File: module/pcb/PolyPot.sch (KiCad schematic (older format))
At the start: 40 parts, among them J1 V_BAT_1S, J2 PROG/DEBUG, J3 HUMIDITY_CONN, J4 TOF_DIST_SENS, J5 M3, J6 M3, J7 M3, J8 M3, J9 LUMINOSITY_CONN, M1 DC_WATER_PUMP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

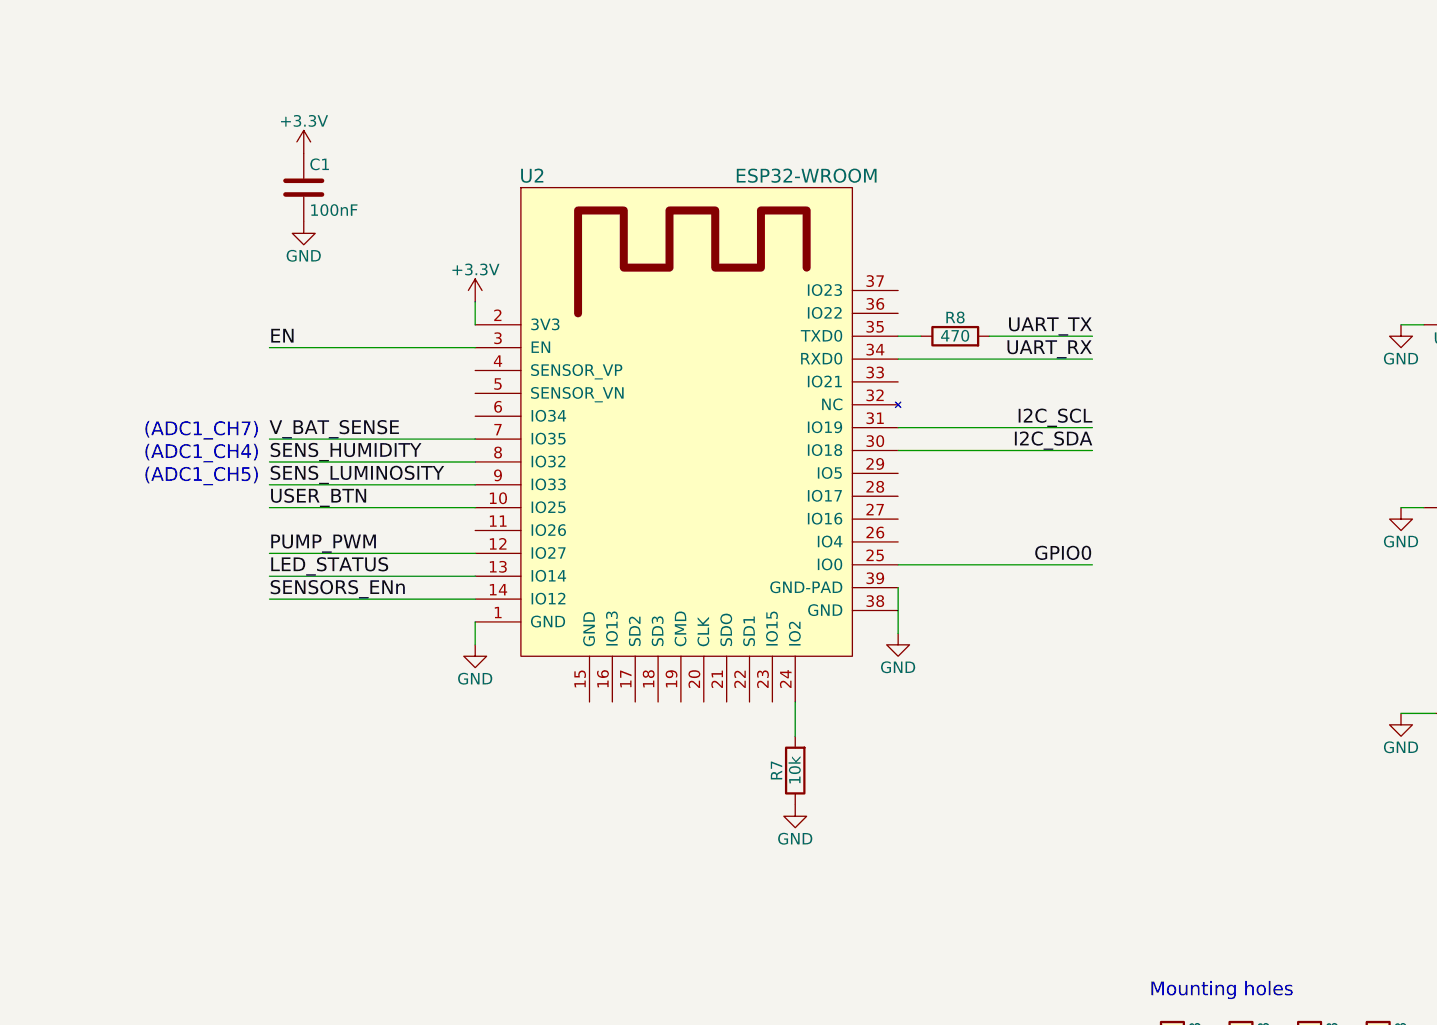
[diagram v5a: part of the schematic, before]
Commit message: Replaced ESP32-WROOM with ESP32-S
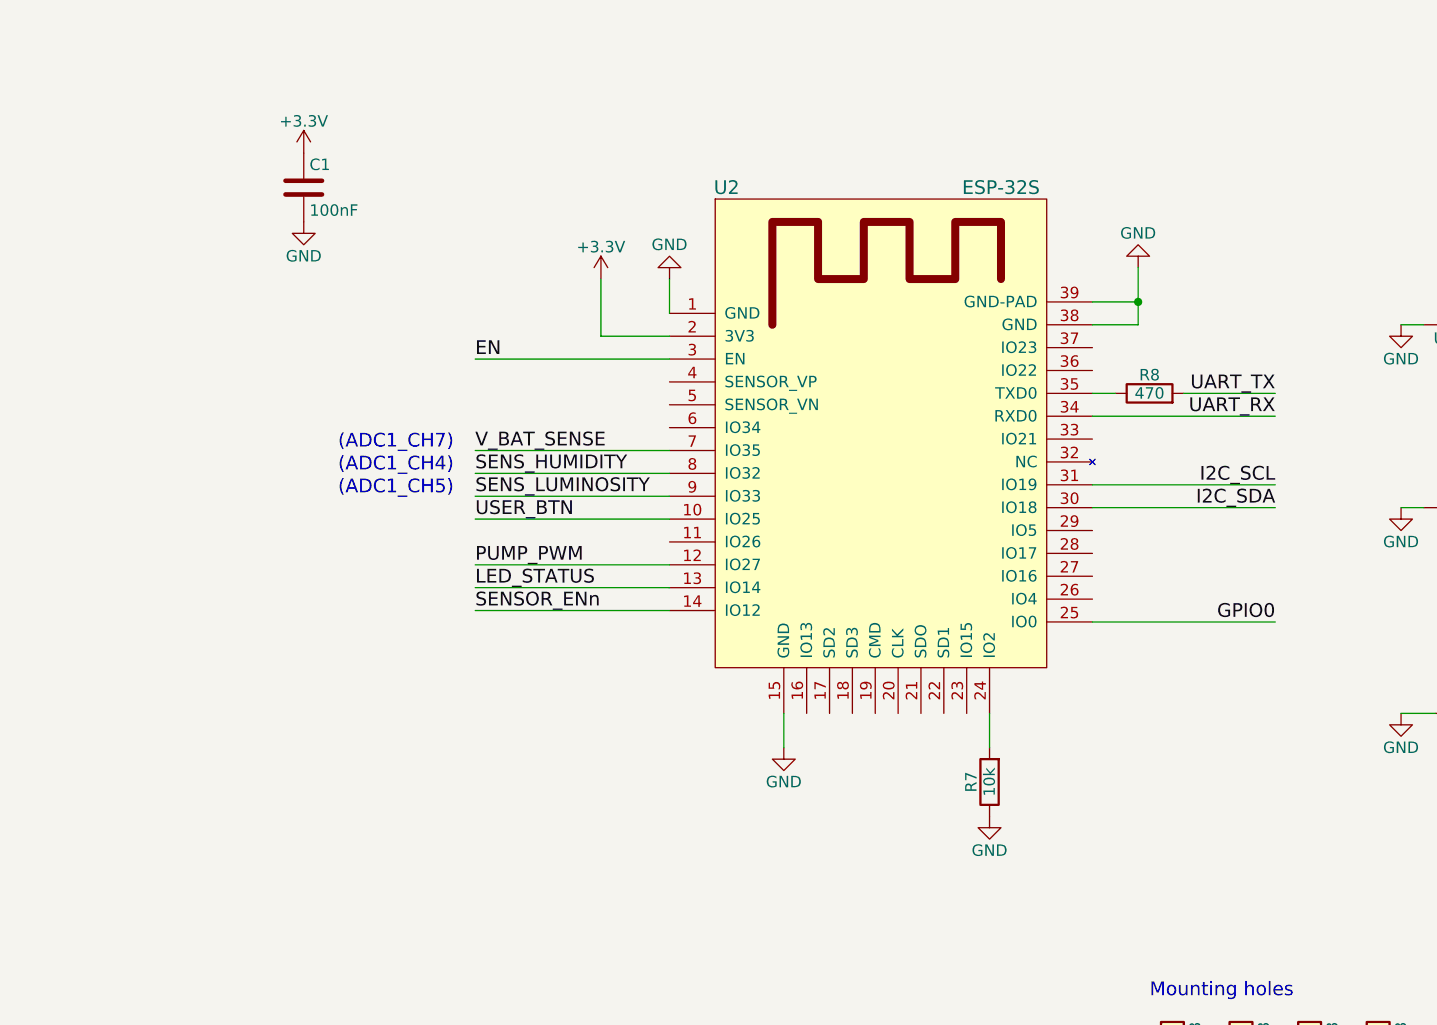
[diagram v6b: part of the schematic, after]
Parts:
- removed U2: ESP32-WROOM, PolyPot:ESP32-WROOM, symbol ESP32-WROOM
- added U2: ESP-32S, ESP32-footprints-Lib:ESP-32S, symbol ESP-32S
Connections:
- net +3V3: now also U2.2 (3V3)
- net EN: now also U2.3 (EN)
- net GND: now also U2.1 (GND), U2.15 (GND), U2.38 (GND), U2.39 (GND-PAD)
- net GPIO0: now also U2.25 (IO0)
- net I2C_SCL: now also U2.31 (IO19)
- net I2C_SDA: now also U2.30 (IO18)
- net LED_STATUS: now also U2.13 (IO14)
- net PUMP_PWM: now also U2.12 (IO27)
- net SENS_HUMIDITY: now also U2.8 (IO32)
- net SENS_LUMINOSITY: now also U2.9 (IO33)
- net UART_RX: now also U2.34 (RXD0)
- net USER_BTN: now also U2.10 (IO25)
- net V_BAT_SENSE: now also U2.7 (IO35)
- net at R7.2: now also U2.24 (IO2)
- net at R8.1: now also U2.35 (TXD0)
- new net SENSOR_ENn: U2.14 (IO12)
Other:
- moved on the sheet: R7, R8

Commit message: Added the PWM driver and routed it on the PCB
There might be some issues with the path for library for ESP32-S. You might need to respecify the path to "ESP32-footprints-Lib.pretty" in the PCB editor library manager.
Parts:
- removed Q1: Q_NMOS_DGS, TO_SOT_Packages_SMD:SOT-23, symbol Q_NMOS_DGS
- added C5: 10uF, Capacitors_SMD:C_0805_HandSoldering, symbol C
- added R10: 10k, Resistors_SMD:R_0603_HandSoldering, symbol R
- added U4: BD6211F-E2, Housings_SOIC:SO-8_5.3x6.2mm_Pitch1.27mm, symbol BD6211F-E2
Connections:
- wire segments 77 -> 88
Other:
- moved on the sheet: JP2, M1, Q2, R2

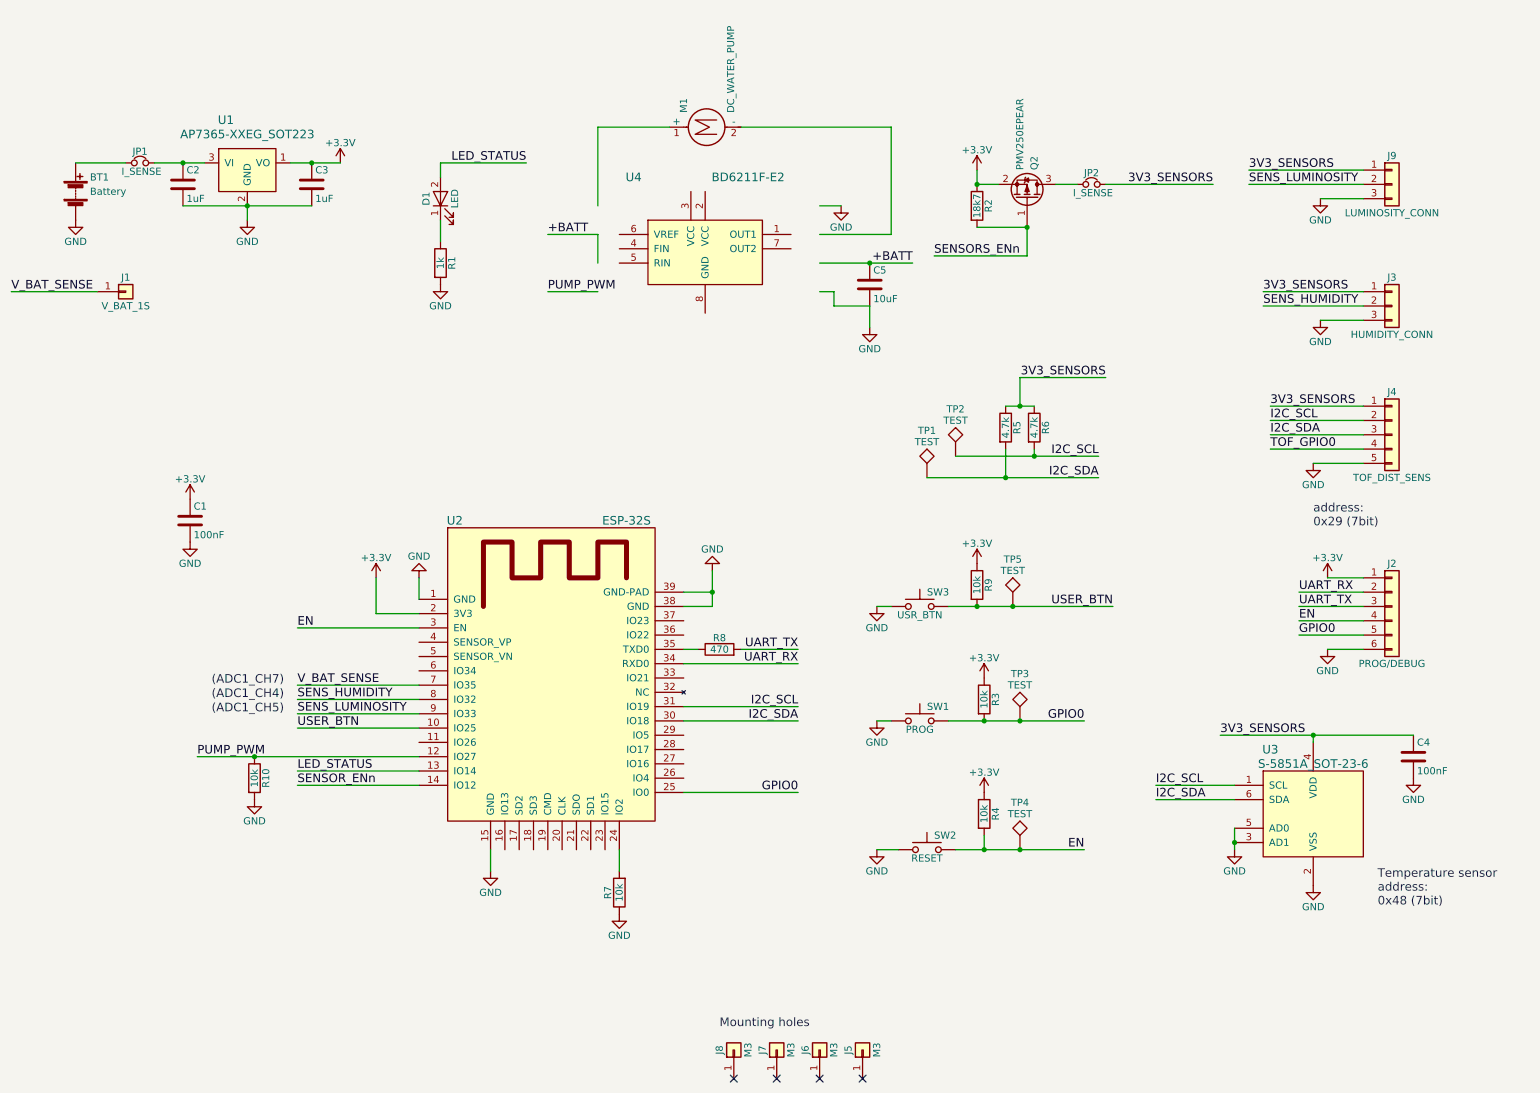
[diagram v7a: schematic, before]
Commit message: PCB: Update footprints, schematic fixes, nicer edge cut, no GND next to antenna
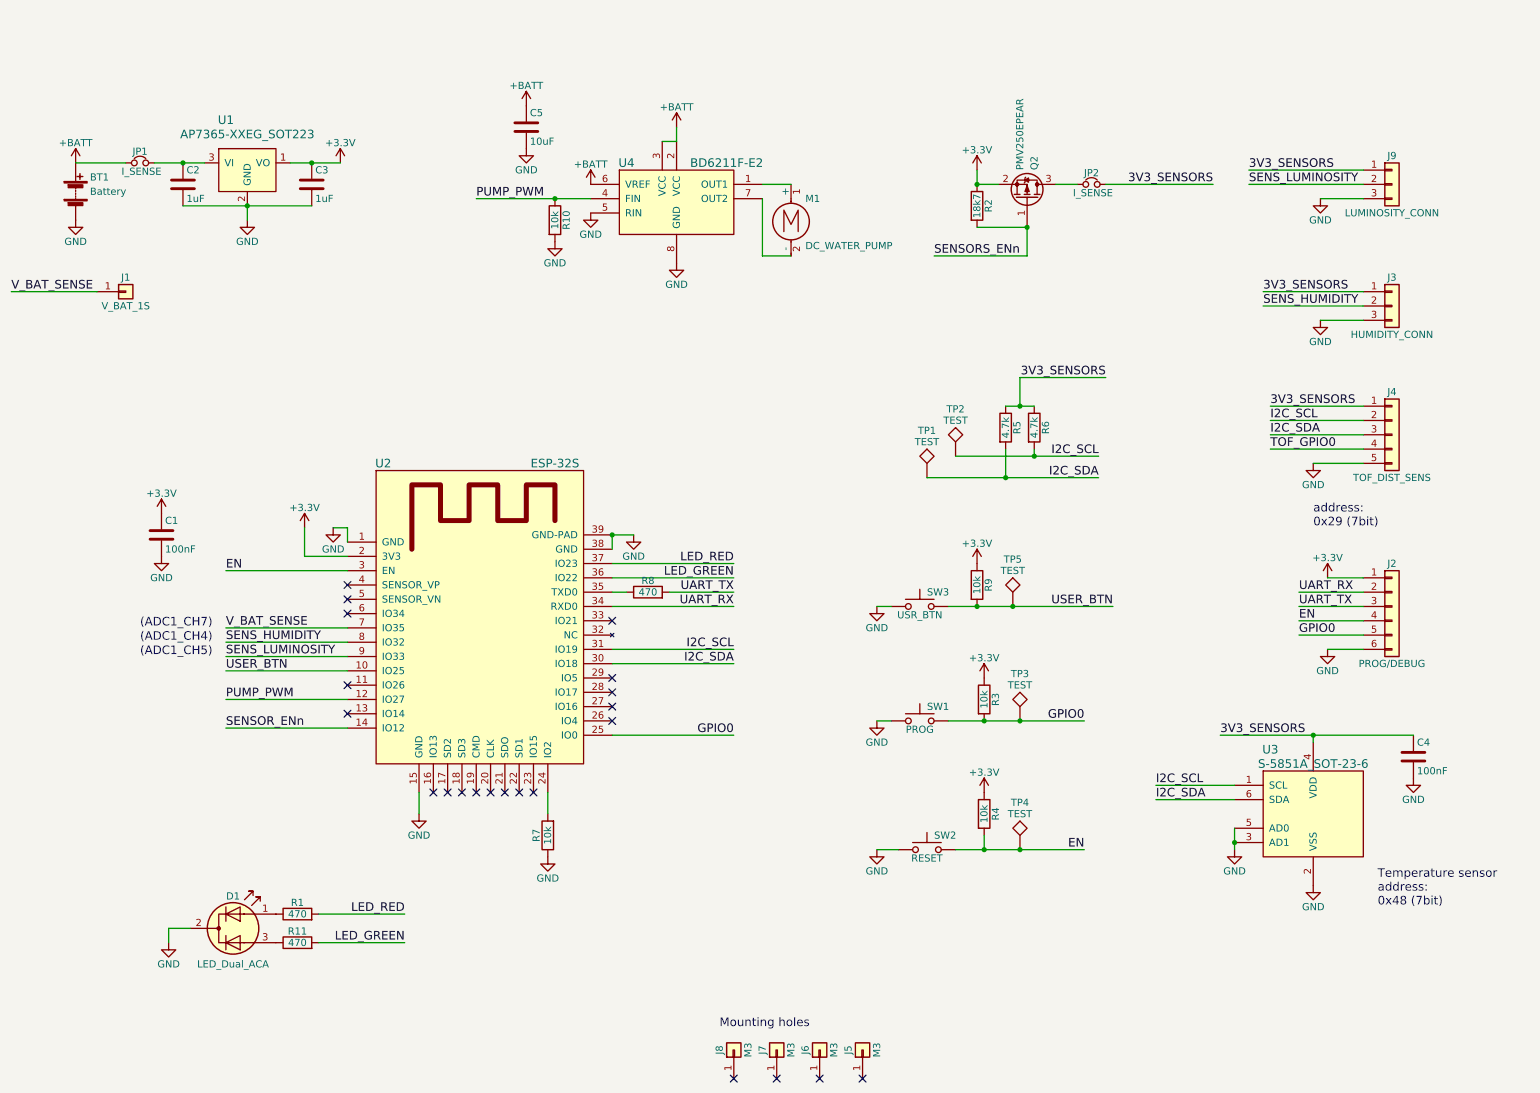
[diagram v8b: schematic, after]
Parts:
- removed D1: LED, LEDs:LED_D3.0mm_Horizontal_O1.27mm_Z2.0mm, symbol LED
- added D1: LED_Dual_ACA, LEDs:LED_D5.0mm-3, symbol LED_Dual_ACA
- added R11: 470, Resistors_SMD:R_0603_HandSoldering, symbol R
- R1: value 1k -> 470
- SW3: footprint Socket_Strips:Socket_Strip_Straight_1x02_Pitch2.00mm -> Buttons_Switches_THT:SW_Tactile_SPST_Angled_PTS645Vx83-2LFS
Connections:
- net labels added: LED_GREEN, LED_RED
- net labels removed: LED_STATUS
- wire segments 88 -> 82
- no-connect marks 4 -> 22
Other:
- moved on the sheet: C1, C5, M1, R1, R10, R7, R8, U2, U4
